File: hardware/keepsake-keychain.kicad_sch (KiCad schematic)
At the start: 1 part

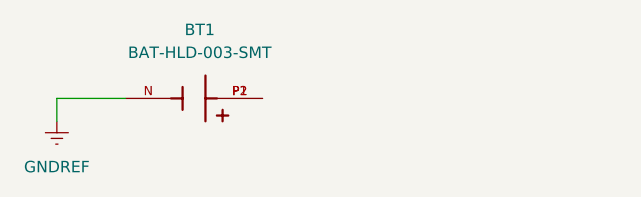
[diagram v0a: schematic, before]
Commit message: Add SPDT switch
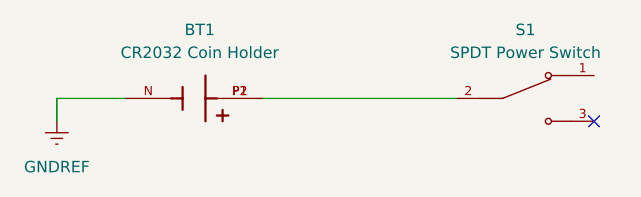
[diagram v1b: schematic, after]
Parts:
- added S1: SPDT Power Switch, SLW-129956-4A-RA-N-D:SW_SLW-129956-4A-RA-N-D, symbol 0_SPST_Switch:SLW-129956-4A-RA-N-D
- BT1: value BAT-HLD-003-SMT -> CR2032 Coin Holder
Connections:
- net at BT1.P1, BT1.P2: now also S1.2
- no-connect marks 0 -> 1
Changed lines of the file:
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@@
 		(rev "1")
+	)
+	(no_connect
+		(at 105.41 53.34)
 	)
 	(wire
@@
 			(width 0)
 			(type default)
+		)
+	)
+	(wire
+		(pts
+			(xy 68.58 50.8) (xy 90.17 50.8)
+		)
+		(stroke
+			(width 0)
+			(type default)
+		)
+	)
+	(symbol
+		(lib_id "0_SPST_Switch:SLW-129956-4A-RA-N-D")
+		(at 97.79 50.8 0)
+		(unit 1)
+		(exclude_from_sim no)
+		(in_bom yes)
+		(on_board yes)
+		(dnp no)
+		(fields_autoplaced yes)
+		(property "Reference" "S1"
+			(at 97.79 43.18 0)
+			(effects
+				(font
+					(size 1.27 1.27)
+				)
+			)
+		)
+		(property "Value" "SPDT Power Switch"
+			(at 97.79 45.72 0)
+			(effects
+				(font
+					(size 1.27 1.27)
+				)
+			)
+		)
+		(property "Footprint" "SLW-129956-4A-RA-N-D:SW_SLW-129956-4A-RA-N-D"
+			(at 97.79 50.8 0)
+			(effects
+				(font
+					(size 1.27 1.27)
+				)
+				(justify bottom)
+				(hide yes)
+			)
+		)
+		(property "Datasheet" ""
+			(at 97.79 50.8 0)
+			(effects
+				(font
+					(size 1.27 1.27)
+				)
+				(hide yes)
+			)
+		)
+		(property "Description" ""
+			(at 97.79 50.8 0)
+			(effects
+				(font
+					(size 1.27 1.27)
+				)
+				(hide yes)
+			)
+		)
+		(property "PARTREV" "1.01"
+			(at 97.79 50.8 0)
+			(effects
+				(font
+					(size 1.27 1.27)
+				)
+				(justify bottom)
+				(hide yes)
+			)
+		)
+		(property "STANDARD" "Manufacturer Recommendations"
+			(at 97.79 50.8 0)
+			(effects
+				(font
+					(size 1.27 1.27)
+				)
+				(justify bottom)
+				(hide yes)
+			)
+		)
+		(property "MAXIMUM_PACKAGE_HEIGHT" "6.3mm"
+			(at 97.79 50.8 0)
+			(effects
+				(font
+					(size 1.27 1.27)
+				)
+				(justify bottom)
+				(hide yes)
+			)
+		)
+		(property "MANUFACTURER" "Same Sky"
+			(at 97.79 50.8 0)
+			(effects
+				(font
+					(size 1.27 1.27)
+				)
+				(justify bottom)
+				(hide yes)
+			)
+		)
+		(pin "2"
+		)
+		(pin "1"
+		)
+		(pin "3"
+		)
+		(instances
+			(project ""
+				(path "/32670795-e352-430d-9b7f-c7f10ebe6399"
+					(reference "S1")
+					(unit 1)
+				)
+			)
 		)
 	)
@@
 			)
 		)
-		(property "Value" "BAT-HLD-003-SMT"
+		(property "Value" "CR2032 Coin Holder"
 			(at 61.595 45.72 0)
 			(effects

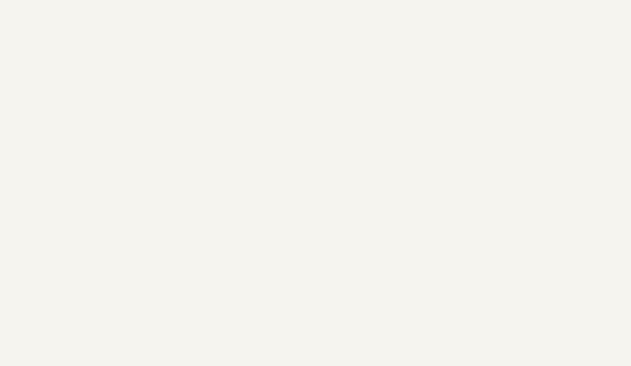
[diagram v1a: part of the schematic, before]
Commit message: Add 74HC595 shift register to lib
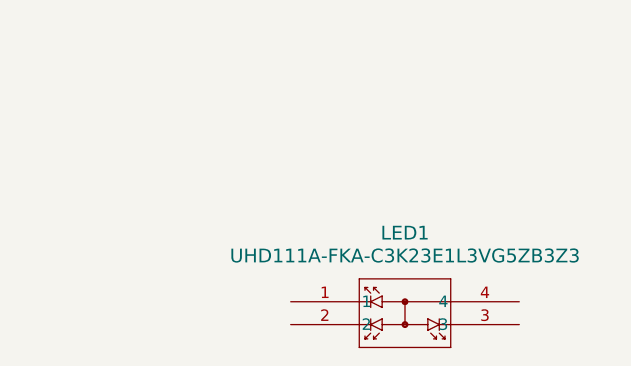
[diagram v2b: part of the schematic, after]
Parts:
- added LED1: UHD111A-FKA-C3K23E1L3VG5ZB3Z3, SMD4_UHD111A-FKA_CRW, symbol 0_RGB_LED:UHD111A-FKA-C3K23E1L3VG5ZB3Z3
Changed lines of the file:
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@@
+	)
+	(symbol
+		(lib_id "0_RGB_LED:UHD111A-FKA-C3K23E1L3VG5ZB3Z3")
+		(at 92.71 96.52 0)
+		(unit 1)
+		(exclude_from_sim no)
+		(in_bom yes)
+		(on_board yes)
+		(dnp no)
+		(fields_autoplaced yes)
+		(property "Reference" "LED1"
+			(at 105.41 88.9 0)
+			(effects
+				(font
+					(size 1.524 1.524)
+				)
+			)
+		)
+		(property "Value" "UHD111A-FKA-C3K23E1L3VG5ZB3Z3"
+			(at 105.41 91.44 0)
+			(effects
+				(font
+					(size 1.524 1.524)
+				)
+			)
+		)
+		(property "Footprint" "SMD4_UHD111A-FKA_CRW"
+			(at 92.71 96.52 0)
+			(effects
+				(font
+					(size 1.27 1.27)
+					(italic yes)
+				)
+				(hide yes)
+			)
+		)
+		(property "Datasheet" "UHD111A-FKA-C3K23E1L3VG5ZB3Z3"
+			(at 92.71 96.52 0)
+			(effects
+				(font
+					(size 1.27 1.27)
+					(italic yes)
+				)
+				(hide yes)
+			)
+		)
+		(property "Description" ""
+			(at 92.71 96.52 0)
+			(effects
+				(font
+					(size 1.27 1.27)
+				)
+				(hide yes)
+			)
+		)
+		(pin "1"
+		)
+		(pin "4"
+		)
+		(pin "2"
+		)
+		(pin "3"
+		)
+		(instances
+			(project ""
+				(path "/32670795-e352-430d-9b7f-c7f10ebe6399"
+					(reference "LED1")
+					(unit 1)
+				)
+			)
+		)
 	)
 	(symbol

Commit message: Add ATtiny1614 IC
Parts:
- added U1: 74HC595PW_118, 74HC595PW_118:SOP65P640X110-16N, symbol 0_74HC595_Shift_Register:74HC595PW_118
- added U2: ATTINY1614-SSF, SOIC14_SL_MCH, symbol 0_ATtiny1614:ATTINY1614-SSF
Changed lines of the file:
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@@
+	)
+	(symbol
+		(lib_id "0_ATtiny1614:ATTINY1614-SSF")
+		(at 176.53 127 0)
+		(unit 1)
+		(exclude_from_sim no)
+		(in_bom yes)
+		(on_board yes)
+		(dnp no)
+		(fields_autoplaced yes)
+		(property "Reference" "U2"
+			(at 214.63 116.84 0)
+			(effects
+				(font
+					(size 1.524 1.524)
+				)
+			)
+		)
+		(property "Value" "ATTINY1614-SSF"
+			(at 214.63 119.38 0)
+			(effects
+				(font
+					(size 1.524 1.524)
+				)
+			)
+		)
+		(property "Footprint" "SOIC14_SL_MCH"
+			(at 176.53 127 0)
+			(effects
+				(font
+					(size 1.27 1.27)
+					(italic yes)
+				)
+				(hide yes)
+			)
+		)
+		(property "Datasheet" "ATTINY1614-SSF"
+			(at 176.53 127 0)
+			(effects
+				(font
+					(size 1.27 1.27)
+					(italic yes)
+				)
+				(hide yes)
+			)
+		)
+		(property "Description" ""
+			(at 176.53 127 0)
+			(effects
+				(font
+					(size 1.27 1.27)
+				)
+				(hide yes)
+			)
+		)
+		(pin "3"
+		)
+		(pin "1"
+		)
+		(pin "2"
+		)
+		(pin "6"
+		)
+		(pin "8"
+		)
+		(pin "4"
+		)
+		(pin "14"
+		)
+		(pin "12"
+		)
+		(pin "9"
+		)
+		(pin "13"
+		)
+		(pin "10"
+		)
+		(pin "7"
+		)
+		(pin "5"
+		)
+		(pin "11"
+		)
+		(instances
+			(project ""
+				(path "/32670795-e352-430d-9b7f-c7f10ebe6399"
+					(reference "U2")
+					(unit 1)
+				)
+			)
+		)
 	)
 	(symbol
@@
 					(unit 1)
 				)
+			)
+		)
+	)
+	(symbol
+		(lib_id "0_74HC595_Shift_Register:74HC595PW_118")
+		(at 77.47 134.62 0)
+		(unit 1)
+		(exclude_from_sim no)
+		(in_bom yes)
+		(on_board yes)
+		(dnp no)
+		(fields_autoplaced yes)
+		(property "Reference" "U1"
+			(at 77.47 114.3 0)
+			(effects
+				(font
+					(size 1.27 1.27)
+				)
+			)
+		)
+		(property "Value" "74HC595PW_118"
+			(at 77.47 116.84 0)
+			(effects
+				(font
+					(size 1.27 1.27)
+				)
+			)
+		)
+		(property "Footprint" "74HC595PW_118:SOP65P640X110-16N"
+			(at 77.47 134.62 0)
+			(effects
+				(font
+					(size 1.27 1.27)
+				)
+				(justify bottom)
+				(hide yes)
+			)
+		)
+		(property "Datasheet" ""
+			(at 77.47 134.62 0)
+			(effects
+				(font
+					(size 1.27 1.27)
+				)
+				(hide yes)
+			)
+		)
+		(property "Description" ""
+			(at 77.47 134.62 0)
+			(effects
+				(font
+					(size 1.27 1.27)
+				)
+				(hide yes)
+			)
+		)
+		(property "MPN" "74HC595PW,118"
+			(at 77.47 134.62 0)
+			(effects
+				(font
+					(size 1.27 1.27)
+				)
+				(justify bottom)
+				(hide yes)
+			)
+		)
+		(property "OC_FARNELL" "1826846"
+			(at 77.47 134.62 0)
+			(effects
+				(font
+					(size 1.27 1.27)
+				)
+				(justify bottom)
+				(hide yes)
+			)
+		)
+		(property "OC_NEWARK" "78R6263"
+			(at 77.47 134.62 0)
+			(effects
+				(font
+					(size 1.27 1.27)
+				)
+				(justify bottom)
+				(hide yes)
+			)
+		)
+		(property "SUPPLIER" "NXP"
+			(at 77.47 134.62 0)
+			(effects
+				(font
+					(size 1.27 1.27)
+				)
+				(justify bottom)
+				(hide yes)
+			)
+		)
+		(property "PACKAGE" "TSSOP-16"
+			(at 77.47 134.62 0)
+			(effects
+				(font
+					(size 1.27 1.27)
+				)
+				(justify bottom)
+				(hide yes)
+			)
+		)
+		(pin "3"
+		)
+		(pin "8"
+		)
+		(pin "12"
+		)
+		(pin "13"
+		)
+		(pin "16"
+		)
+		(pin "10"
+		)
+		(pin "11"
+		)
+		(pin "14"
+		)
+		(pin "1"
+		)
+		(pin "15"
+		)
+		(pin "2"
+		)
+		(pin "4"
+		)
+		(pin "5"
+		)
+		(pin "6"
+		)
+		(pin "9"
+		)
+		(pin "7"
+		)
+		(instances
+			(project ""
+				(path "/32670795-e352-430d-9b7f-c7f10ebe6399"
+					(reference "U1")
+					(unit 1)
+				)

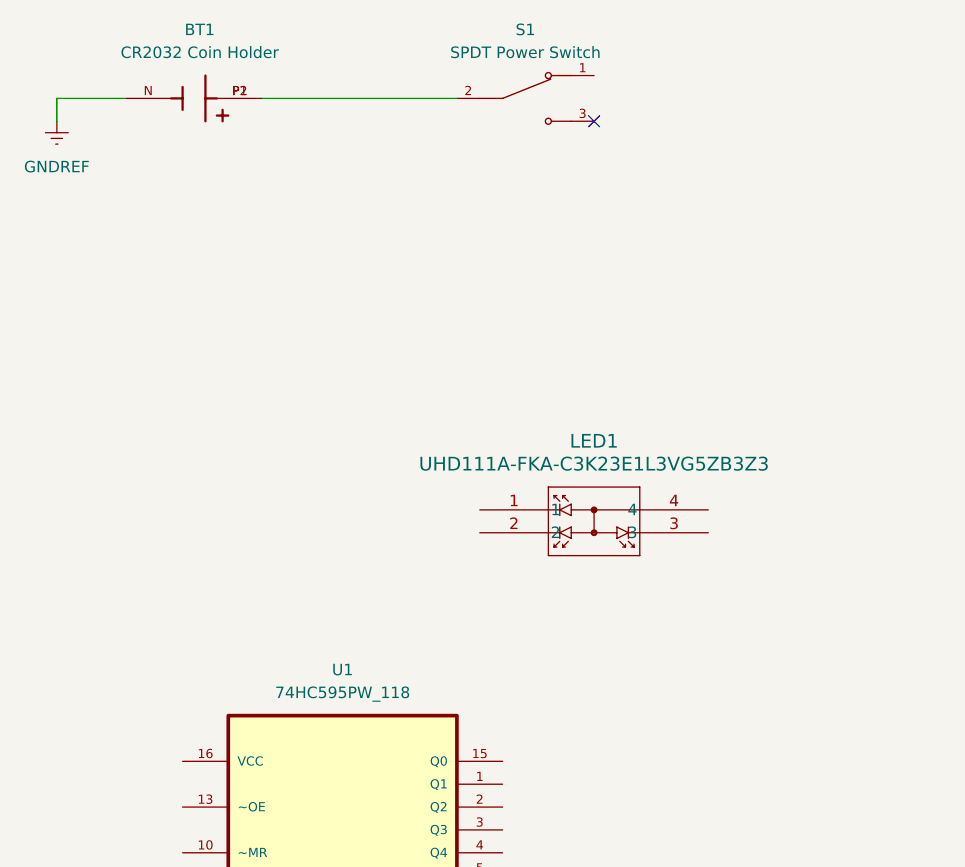
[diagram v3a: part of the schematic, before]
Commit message: Restructure component library
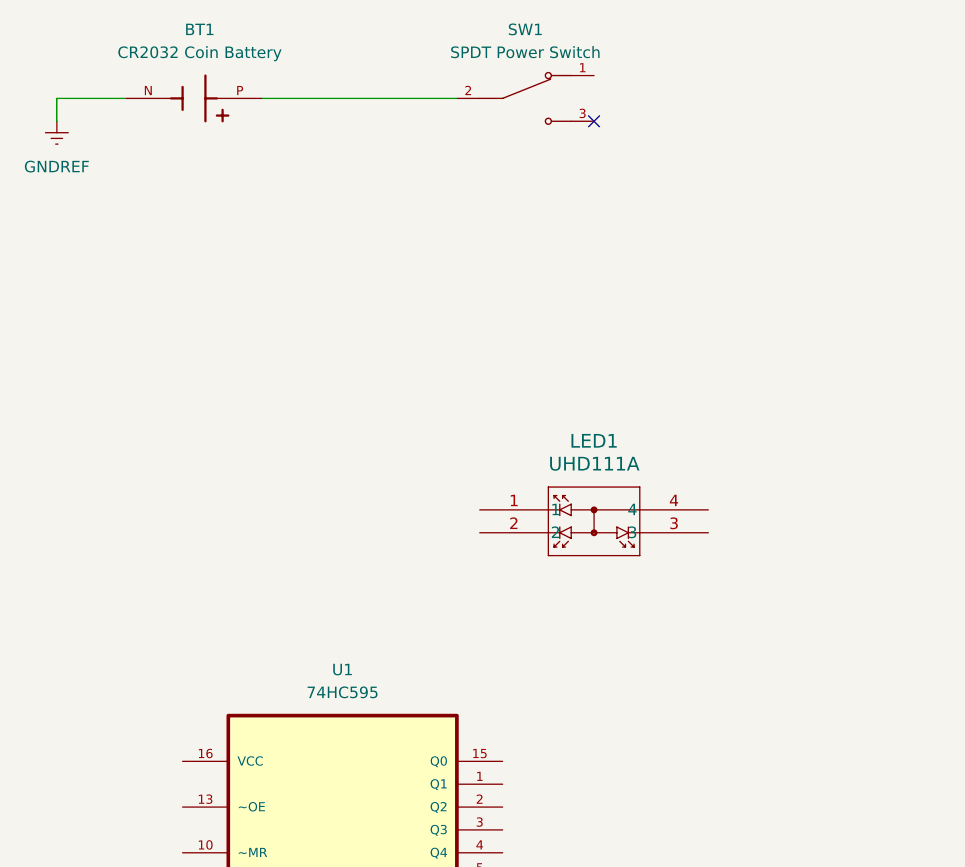
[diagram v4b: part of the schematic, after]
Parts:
- removed BT1: CR2032 Coin Holder, BAT-HLD-003-SMT:BAT_BAT-HLD-003-SMT, symbol 0_Button_Cell_Holder:BAT-HLD-003-SMT
- added BT1: CR2032 Coin Battery, BH-25C-1:BAT_BH-25C-1, symbol 0_Button_Cell_Holder:BH-25C-1
- LED1: value UHD111A-FKA-C3K23E1L3VG5ZB3Z3 -> UHD111A
- U1: value 74HC595PW_118 -> 74HC595
- renumbered S1 to SW1
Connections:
- net GNDREF: now also BT1.N
- net at SW1.2: now also BT1.P
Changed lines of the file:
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@@
 			)
 		)
-		(property "Value" "UHD111A-FKA-C3K23E1L3VG5ZB3Z3"
+		(property "Value" "UHD111A"
 			(at 105.41 91.44 0)
 			(effects
@@
 		(dnp no)
 		(fields_autoplaced yes)
-		(property "Reference" "S1"
+		(property "Reference" "SW1"
 			(at 97.79 43.18 0)
 			(effects
@@
 			(project ""
 				(path "/32670795-e352-430d-9b7f-c7f10ebe6399"
-					(reference "S1")
+					(reference "SW1")
 					(unit 1)
 				)
@@
 			)
 		)
-		(property "Value" "74HC595PW_118"
+		(property "Value" "74HC595"
 			(at 77.47 116.84 0)
 			(effects
@@
 	)
 	(symbol
-		(lib_id "0_Button_Cell_Holder:BAT-HLD-003-SMT")
+		(lib_id "0_Button_Cell_Holder:BH-25C-1")
 		(at 60.96 50.8 180)
 		(unit 1)
@@
 			)
 		)
-		(property "Value" "CR2032 Coin Holder"
+		(property "Value" "CR2032 Coin Battery"
 			(at 61.595 45.72 0)
 			(effects
@@
 			)
 		)
-		(property "Footprint" "BAT-HLD-003-SMT:BAT_BAT-HLD-003-SMT"
+		(property "Footprint" "BH-25C-1:BAT_BH-25C-1"
 			(at 60.96 50.8 0)
 			(effects
@@
 			)
 		)
-		(property "SnapEDA_Link" "https://www.snapeda.com/parts/BAT-HLD-003-SMT/Linx/view-part/?ref=snap"
-			(at 60.96 50.8 0)
-			(effects
-				(font
-					(size 1.27 1.27)
-				)
-				(justify bottom)
-				(hide yes)
-			)
-		)
-		(property "Check_prices" "https://www.snapeda.com/parts/BAT-HLD-003-SMT/Linx/view-part/?ref=eda"
-			(at 60.96 50.8 0)
-			(effects
-				(font
-					(size 1.27 1.27)
-				)
-				(justify bottom)
-				(hide yes)
-			)
-		)
-		(property "Package" "None"
-			(at 60.96 50.8 0)
-			(effects
-				(font
-					(size 1.27 1.27)
-				)
-				(justify bottom)
-				(hide yes)
-			)
-		)
-		(property "Price" "None"
-			(at 60.96 50.8 0)
-			(effects
-				(font
-					(size 1.27 1.27)
-				)
-				(justify bottom)
-				(hide yes)
-			)
-		)
-		(property "MF" "Linx Technologies Inc."
-			(at 60.96 50.8 0)
-			(effects
-				(font
-					(size 1.27 1.27)
-				)
-				(justify bottom)
-				(hide yes)
-			)
-		)
-		(property "MP" "BAT-HLD-003-SMT"
-			(at 60.96 50.8 0)
-			(effects
-				(font
-					(size 1.27 1.27)
-				)
-				(justify bottom)
-				(hide yes)
-			)
-		)
-		(property "Purchase-URL" "https://www.snapeda.com/api/url_track_click_mouser/?unipart_id=6393643&manufacturer=Linx Technologies Inc.&part_name=BAT-HLD-003-SMT&search_term=None"
-			(at 60.96 50.8 0)
-			(effects
-				(font
-					(size 1.27 1.27)
-				)
-				(justify bottom)
-				(hide yes)
-			)
-		)
-		(property "Availability" "In Stock"
-			(at 60.96 50.8 0)
-			(effects
-				(font
-					(size 1.27 1.27)
-				)
-				(justify bottom)
-				(hide yes)
-			)
-		)
-		(property "Description_1" "Battery Holder Coin 20 SMT Nickel"
-			(at 60.96 50.8 0)
-			(effects
-				(font
-					(size 1.27 1.27)
-				)
-				(justify bottom)
-				(hide yes)
-			)
-		)
-		(pin "P1"
+		(property "PARTREV" ""
+			(at 60.96 50.8 0)
+			(effects
+				(font
+					(size 1.27 1.27)
+				)
+				(justify bottom)
+				(hide yes)
+			)
+		)
+		(property "STANDARD" "Manufacturer Recommendations"
+			(at 60.96 50.8 0)
+			(effects
+				(font
+					(size 1.27 1.27)
+				)
+				(justify bottom)
+				(hide yes)
+			)
+		)
+		(property "MAXIMUM_PACKAGE_HEIGHT" "8.7mm"
+			(at 60.96 50.8 0)
+			(effects
+				(font
+					(size 1.27 1.27)
+				)
+				(justify bottom)
+				(hide yes)
+			)
+		)
+		(property "MANUFACTURER" "Adam Tech"
+			(at 60.96 50.8 0)
+			(effects
+				(font
+					(size 1.27 1.27)
+				)
+				(justify bottom)
+				(hide yes)
+			)
+		)
+		(pin "P"
 		)
 		(pin "N"
 		)
-		(pin "P2"
-		)
 		(instances
